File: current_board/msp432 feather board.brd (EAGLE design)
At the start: 57.2 x 22.9 mm, 53 parts, among them IC1 FT232RL, J1 1981568-1, J2 B2B-PH-SM4-TB(LF)(SN), U1 DMG3415U-7X2-DFN2015-3, U2 MCP73831T-2ACI/OT, X1 TSW-116-07-G-S, X2 TSW-116-07-G-S, Y1 ECS-480-10-37-JTN-TR

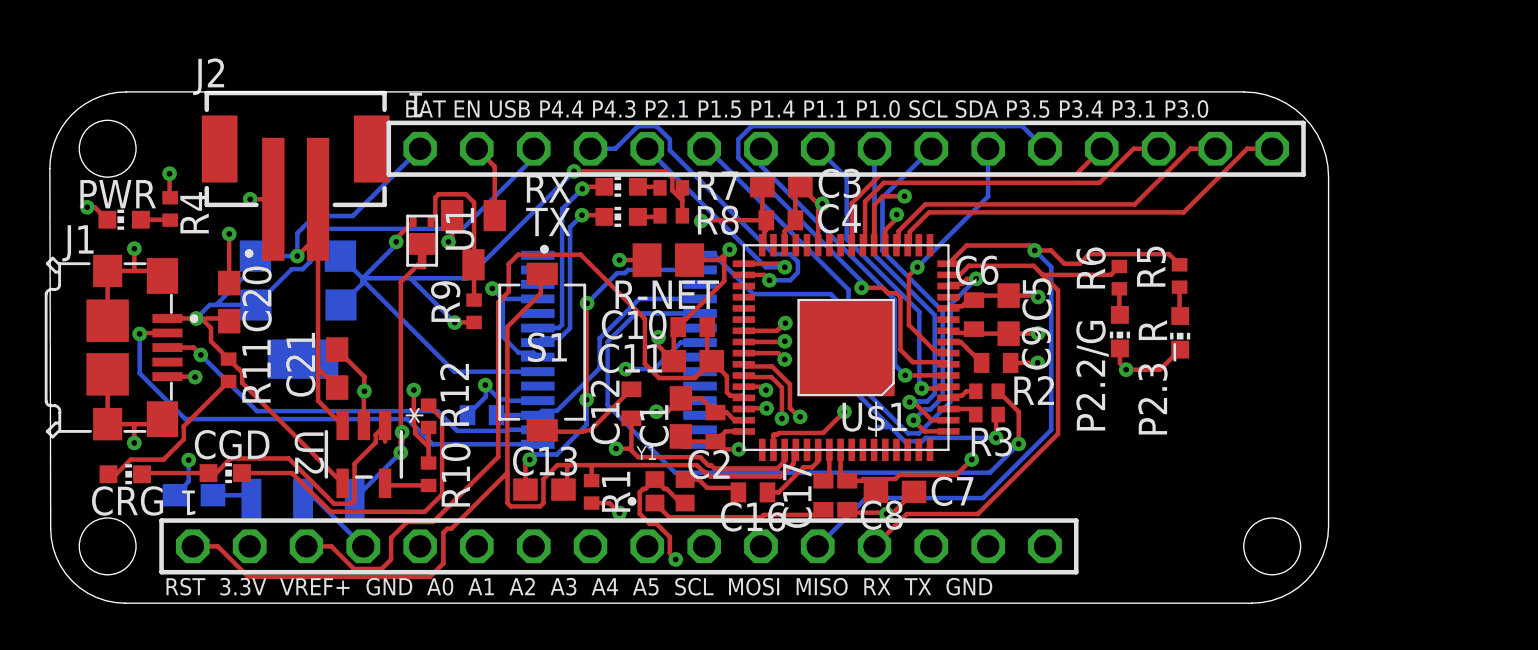
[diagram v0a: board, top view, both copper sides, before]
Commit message: updated board file
Fixed issue with floating TEST pin on FT232RL IC
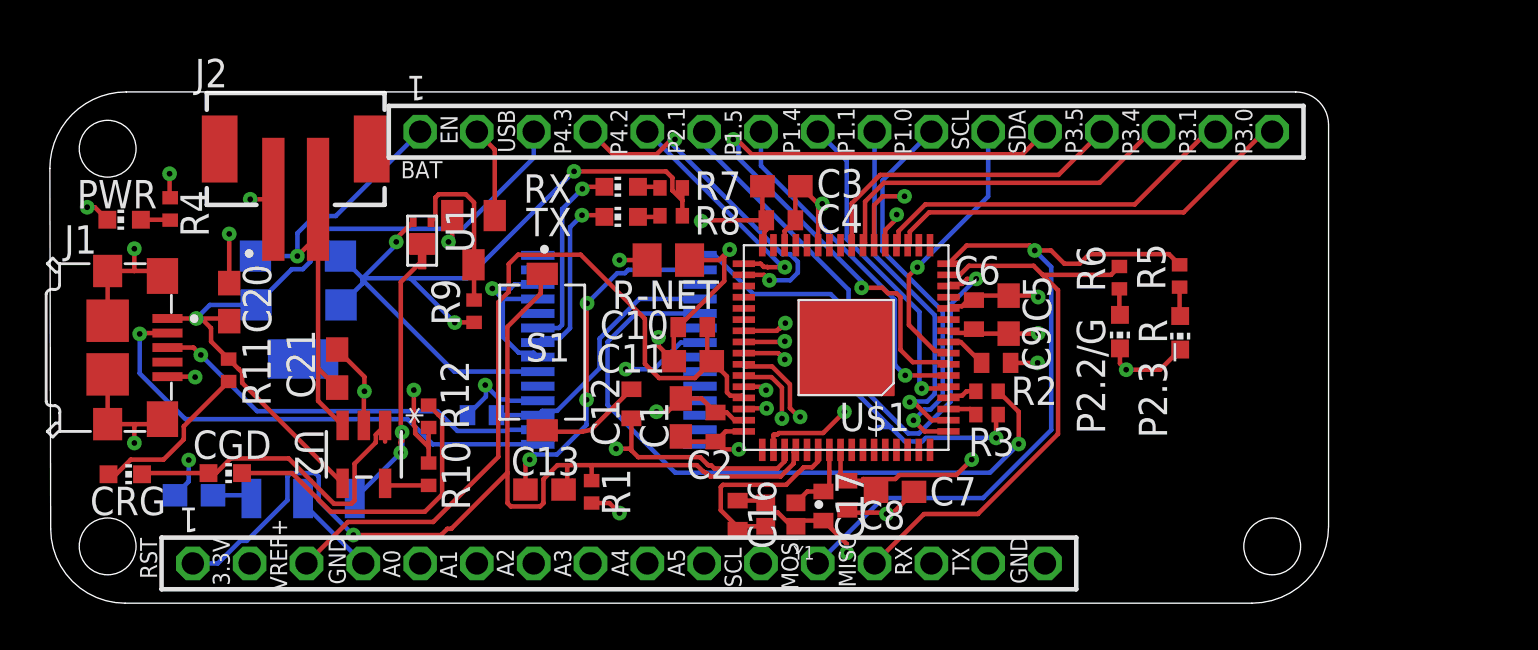
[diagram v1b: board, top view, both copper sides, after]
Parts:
- C10: value 50nF -> 47nF
- C11: value 5uF -> 4.7uF
- R9: value (none) -> 100K
- moved Y1 5.06 mm to (32.6, 3.96), turned to 180 degrees
- moved C16 1.23 mm to (30.7, 3.94), turned to 90 degrees
- moved X2 0.76 mm to (35.6, 21.1)
- moved X1 0.76 mm to (25.4, 1.78)
- moved C17 0.48 mm to (34.5, 4.34), turned to 270 degrees
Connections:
- removed net N$45: C17.1, Y1.1
- removed net N$46: C16.1, Y1.3
- removed net P4.4: U$1.34, X2.4
- new net P4.2: U$1.33, X2.5
- net GND: now also C16.2, C17.2, IC1.26
- net N$47: now also C16.1, Y1.3; no longer C16.2
- net N$48: now also C17.1, Y1.1; no longer C17.2
- net P4.3: now also U$1.34, X2.4; no longer U$1.33, X2.5
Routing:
- net P4.4: track 15.6 -> 0.00 mm, vias 1 -> 0
- net P4.2: track 0.00 -> 10.6 mm, vias 0 -> 1
- net N$45: track 7.93 -> 0.00 mm
- net P4.3: track 10.2 -> 15.9 mm, vias 1 -> 2
- net N$47: track 3.35 -> 8.88 mm
- net N$46: track 2.62 -> 0.00 mm
- net GND: track 97.6 -> 99.9 mm
- net RST: track 46.0 -> 47.9 mm, vias 0 -> 1
- net N$48: track 1.49 -> 3.41 mm
- net VREF+: track 37.6 -> 36.5 mm
- net VUSB: track 33.5 -> 32.6 mm
- net P1.1: track 15.4 -> 16.2 mm
- net SCL: track 11.6 -> 12.4 mm
- net RX: track 17.8 -> 18.5 mm
- net P1.5: track 14.7 -> 15.5 mm
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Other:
- outline, holes or cut-outs redrawn
- board text added: "3.3V"
- board text added: "A0"
- board text added: "A1"
- board text added: "A2"
- board text added: "A3"
- board text added: "A4"
- board text added: "A5"
- board text added: "BAT"
- board text added: "EN"
- board text added: "GND"
- board text added: "MISO"
- board text added: "MOSI"
- board text added: "P1.0"
- board text added: "P1.1"
- board text added: "P1.4"
- board text added: "P1.5"
- board text added: "P2.1"
- board text added: "P3.0"
- board text added: "P3.1"
- board text added: "P3.4"
- board text added: "P3.5"
- board text added: "P4.2"
- board text added: "P4.3"
- board text added: "RST"
- board text added: "RX"
- board text added: "SCL"
- board text added: "SDA"
- board text added: "TX"
- board text added: "USB"
- board text added: "VREF+"
- board text removed: "BAT EN USB P4.4 P4.3 P2.1 P1.5 P1.4 P1.1 P1.0 SCL SDA P3.5 P3.4 P3.1 P3.0"
- board text removed: "RST 3.3V VREF+ GND A0 A1 A2 A3 A4 A5 SCL MOSI MISO RX TX GND"

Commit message: Add files via upload
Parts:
- removed P2.3_R: (no value), led:CHIP-LED0603
- added J3: (no value), SparkFun-Connectors:1X04_NO_SILK
- added P2.3/R: (no value), led:CHIP-LED0603
- IC1: device ftdichip:SSOP28 -> FT232RL:SSOP28-LD
- moved R5 2.80 mm to (47.8, 14.0)
- moved R6 1.58 mm to (46.3, 14.0)
- moved P2.2/G 1.57 mm to (46.3, 11.7)
- moved C7 0.64 mm to (37.8, 4.34)
- moved C6 0.31 mm to (41.6, 12.9)
- moved C3 0.30 mm to (32.7, 18.9)
- moved C5 0.30 mm to (43.1, 12.9)
- moved C4 0.28 mm to (32.6, 17.4)
- moved U$3 0.23 mm to (19.1, 16.3)
- moved R2 0.23 mm to (42.1, 9.47)
- moved R3 0.23 mm to (42.1, 8.43)
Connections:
- net N$5 renamed DM
- net N$6 renamed DP
- new net TCK: J3.2, U$1.64
- new net TDI: J3.3, U$1.61
- new net TDO: J3.4, U$1.62
- new net TMS: J3.1, U$1.63
- net 5V+: no longer IC1.20
- net GND: now also P2.3/R.C; no longer P2.3_R.C
- net N$11: now also IC1.22; no longer IC1.23
- net N$12: now also IC1.23; no longer IC1.22
- net N$3: now also IC1.3; no longer IC1.2
- net N$42: now also P2.3/R.A; no longer P2.3_R.A
- net N$7: now also IC1.5; no longer IC1.1
- net N$8: now also IC1.1; no longer IC1.5
- net VIN: now also IC1.20
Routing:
- net TMS: track 0.00 -> 26.4 mm, vias 0 -> 1
- net TDI: track 0.00 -> 23.4 mm, vias 0 -> 2
- net TDO: track 0.00 -> 22.0 mm, vias 0 -> 1
- net TCK: track 0.00 -> 20.2 mm, vias 0 -> 1
- net VIN: track 13.3 -> 28.1 mm
- net 5V+: track 38.1 -> 28.7 mm
- net N$8: track 30.4 -> 36.3 mm
- net N$3: track 15.7 -> 21.4 mm
- net +3.3V: track 26.9 -> 30.6 mm, vias 6 -> 7
- net A0: track 23.3 -> 21.8 mm
- net MOSI: track 32.6 -> 31.2 mm
- net A1: track 21.5 -> 20.1 mm
- net N$11: track 8.62 -> 10.0 mm
- net GND: track 99.9 -> 98.5 mm
- net +5V: track 2.01 -> 3.32 mm
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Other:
- board text added: "Designed By Seth Kerr Updated: 07/28/2020 OpenSource https://github.com/skerr92/msp432-feather"
- board text added: "JTAG"
- board text added: "MSP432 Long Feather"
- board text added: "TCK"
- board text added: "TDI"
- board text added: "TDO"
- board text added: "TMS"

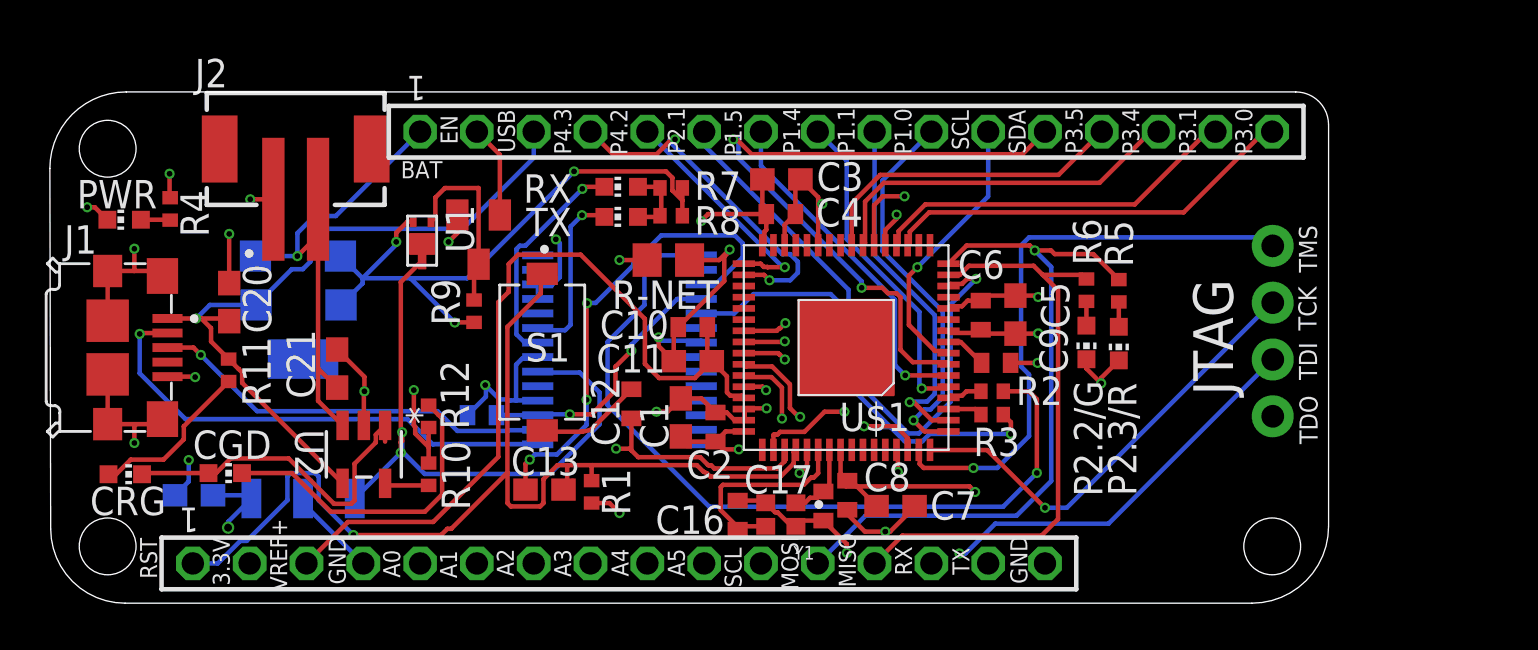
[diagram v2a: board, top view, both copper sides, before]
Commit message: Add files via upload
fixing JTAG and adding ARM 10pin JTAG connector
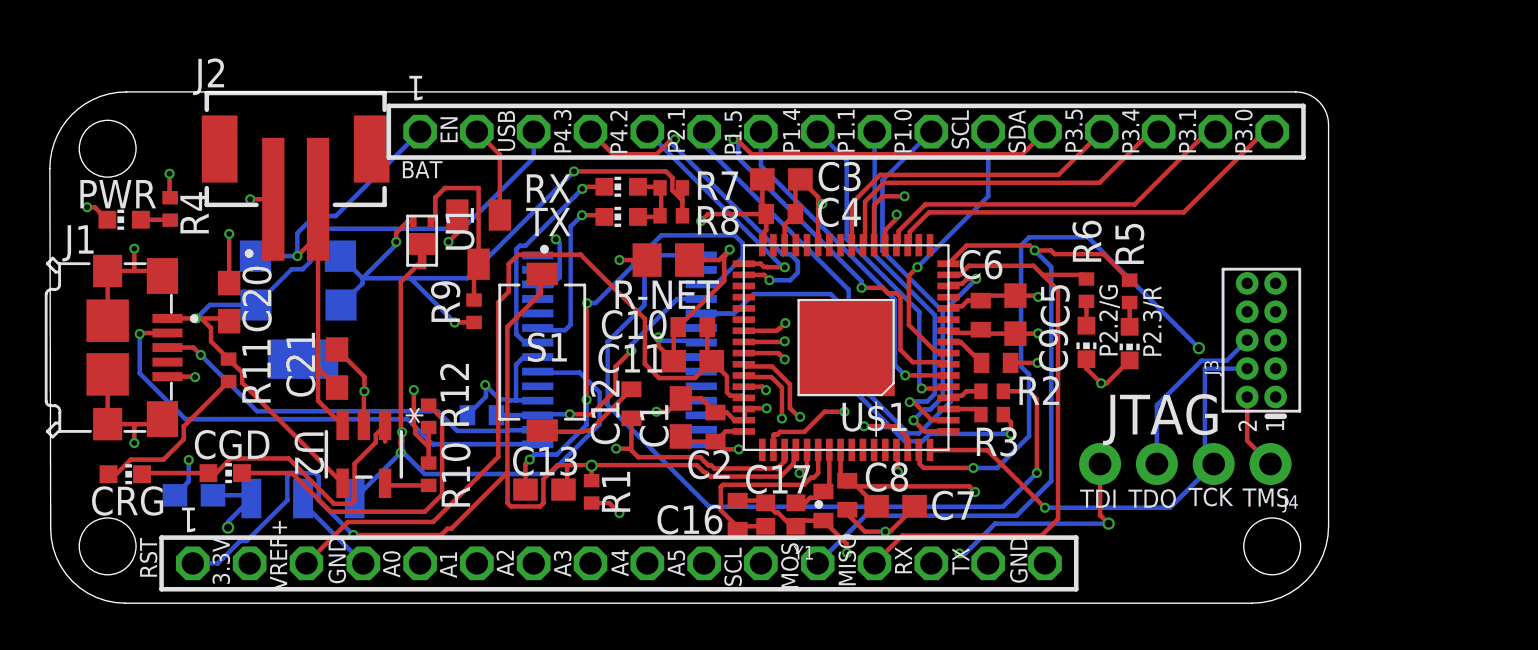
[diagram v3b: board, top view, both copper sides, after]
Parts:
- added J4: (no value), SparkFun-Connectors:1X04_NO_SILK
- J3: value (none) -> CORTEX_JTAG_DEBUG_MINIMUM_PTH; device SparkFun-Connectors:1X04_NO_SILK -> SparkFun-Connectors:2X5-PTH-1.27MM
- moved J3 4.25 mm to (54.1, 11.8), turned to 90 degrees
- moved R5 0.48 mm to (48.2, 13.9)
- moved P2.3/R 0.48 mm to (48.2, 11.6)
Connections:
- net +3.3V: now also J3.1
- net GND: now also J3.3, J3.5, J3.9
- net RST: now also J3.10
- net TCK: now also J3.4, J4.2; no longer J3.2
- net TDI: now also J4.4; no longer J3.3
- net TDO: now also J3.6, J4.3; no longer J3.4
- net TMS: now also J3.2, J4.1; no longer J3.1
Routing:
- net RST: track 47.9 -> 81.2 mm, vias 1 -> 2
- net TDO: track 22.0 -> 29.9 mm
- net TDI: track 23.4 -> 15.9 mm, vias 2 -> 3
- net TMS: track 26.4 -> 31.6 mm, vias 1 -> 2
- net TCK: track 20.2 -> 20.9 mm
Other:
- board text added: "2 1"

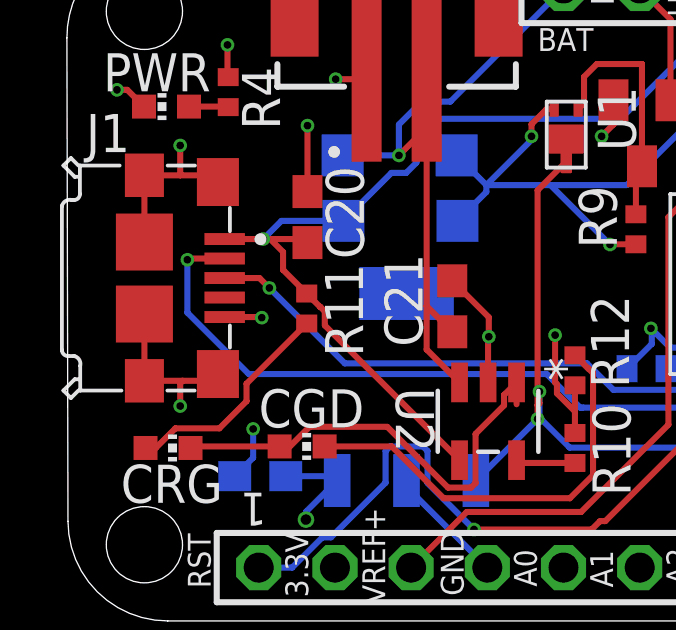
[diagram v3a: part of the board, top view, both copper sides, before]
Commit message: Add files via upload
wiring issues with the USB interface.
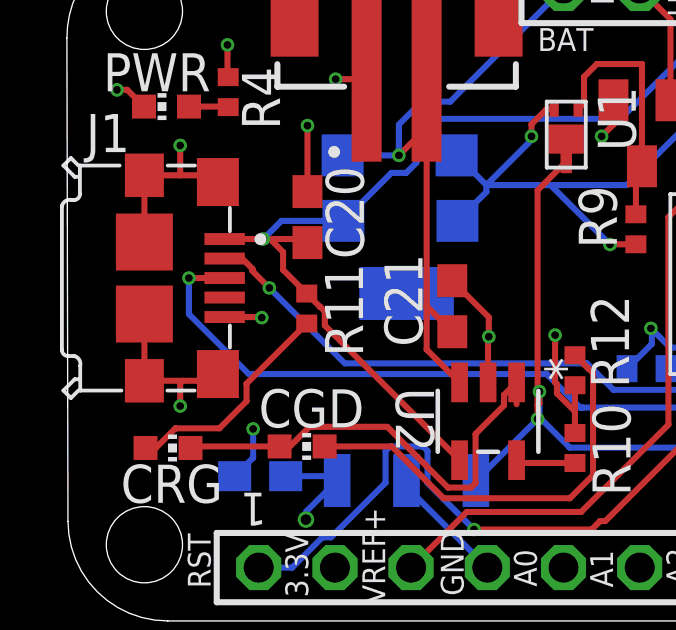
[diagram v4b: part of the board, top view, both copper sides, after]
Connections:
- net DM: now also J1.2; no longer J1.3
- net DP: now also J1.3; no longer J1.2
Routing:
- net DP: track 22.1 -> 21.5 mm
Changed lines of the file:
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@@
 <drawing>
 <settings>
-<setting alwaysvectorfont="yes"/>
+<setting alwaysvectorfont="no"/>
 <setting verticaltext="up"/>
 </settings>
@@
 <signal name="DM">
 <contactref element="IC1" pad="16"/>
-<contactref element="J1" pad="3"/>
-<wire x1="5.215" y1="11.43" x2="6.3754" y2="11.43" width="0.2032" layer="1"/>
-<wire x1="6.3754" y1="11.43" x2="6.7056" y2="11.0998" width="0.2032" layer="1"/>
 <via x="6.7056" y="11.0998" extent="1-16" drill="0.254"/>
 <wire x1="6.7056" y1="11.0998" x2="9.2202" y2="8.5852" width="0.2032" layer="16"/>
@@
 <wire x1="21.6916" y1="7.7343" x2="21.7694" y2="7.7534" width="0.2032" layer="16"/>
 <wire x1="20.447" y1="7.7343" x2="20.3838125" y2="7.7034" width="0.2032" layer="16"/>
+<contactref element="J1" pad="2"/>
+<wire x1="6.144" y1="11.6614" x2="6.144" y2="11.7352125" width="0.2032" layer="1"/>
+<wire x1="6.144" y1="11.7352125" x2="5.7992125" y2="12.08" width="0.2032" layer="1"/>
+<wire x1="5.7992125" y1="12.08" x2="5.215" y2="12.08" width="0.2032" layer="1"/>
+<wire x1="6.7056" y1="11.0998" x2="6.144" y2="11.6614" width="0.2032" layer="1"/>
 </signal>
 <signal name="DP">
 <contactref element="IC1" pad="15"/>
-<contactref element="J1" pad="2"/>
 <wire x1="17.0755875" y1="7.1034" x2="15.9493875" y2="8.2296" width="0.2032" layer="16"/>
 <wire x1="15.9493875" y1="8.2296" x2="6.0198" y2="8.2296" width="0.2032" layer="16"/>
-<wire x1="3.9726" y1="10.2768" x2="3.9726" y2="12.0396" width="0.2032" layer="16"/>
-<via x="3.9726" y="12.0396" extent="1-16" drill="0.254"/>
-<wire x1="3.9726" y1="12.0396" x2="4.013" y2="12.08" width="0.2032" layer="1"/>
-<wire x1="4.013" y1="12.08" x2="5.215" y2="12.08" width="0.2032" layer="1"/>
-<wire x1="6.0198" y1="8.2296" x2="3.9726" y2="10.2768" width="0.2032" layer="16"/>
+<wire x1="4.0234" y1="10.226" x2="4.0234" y2="11.43" width="0.2032" layer="16"/>
+<via x="4.0234" y="11.43" extent="1-16" drill="0.254"/>
+<wire x1="4.0234" y1="11.43" x2="4.0638" y2="11.4704" width="0.2032" layer="1"/>
+<wire x1="6.0198" y1="8.2296" x2="4.0234" y2="10.226" width="0.2032" layer="16"/>
 <wire x1="17.1577" y1="7.112" x2="21.6916" y2="7.112" width="0.2032" layer="16"/>
 <wire x1="21.6916" y1="7.112" x2="21.7694" y2="7.1034" width="0.2032" layer="16"/>
 <wire x1="17.1577" y1="7.112" x2="17.0755875" y2="7.1034" width="0.2032" layer="16"/>
+<contactref element="J1" pad="3"/>
+<wire x1="4.0234" y1="11.43" x2="5.215" y2="11.43" width="0.2032" layer="1"/>
 </signal>
 <signal name="TMS">
